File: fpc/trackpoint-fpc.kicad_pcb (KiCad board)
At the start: 2 copper layers, 10.2 x 25.4 mm, 3 parts, among them P1 CONN_8, P2 CONN_5, P3 CONN_8

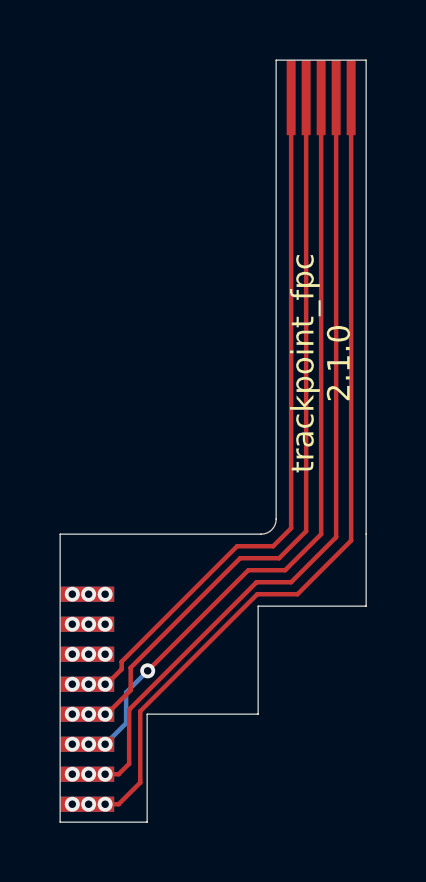
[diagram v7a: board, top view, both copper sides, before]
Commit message: Update FPC CAD and bump its version to 2.2.0
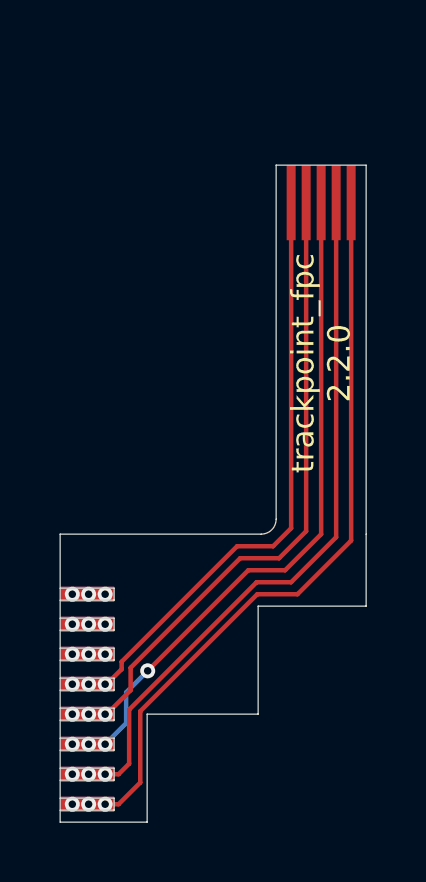
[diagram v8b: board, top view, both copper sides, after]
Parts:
- moved P2 3.50 mm to (198.3, 128.7)
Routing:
- net /DATA: track 22.8 -> 18.2 mm
- net /VCC: track 28.0 -> 23.4 mm
- net /RESET: track 25.3 -> 20.8 mm
- net /GND: track 26.6 -> 22.1 mm
- net /CLK: track 23.9 -> 19.5 mm
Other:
- board size 10.2 x 25.4 mm -> 10.2 x 21.9 mm
- board text added: "trackpoint_fpc 2.2.0"
- board text removed: "trackpoint_fpc 2.1.0"
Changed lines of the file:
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@@
   (general
     (thickness 1.6)
-    (drawings 30)
+    (drawings 54)
     (tracks 59)
     (zones 0)
@@
   (title_block
     (title "UHK Trackpoint FPC")
-    (rev 2.1.0)
+    (rev 2.2.0)
     (company "Ultimate Gadget Laboratories Kft.")
   )
@@
   )
   (module UGL:Trackpoint_FPC_5x0.5_pads (layer F.Cu)
-    (at 198.3 125.15)
+    (at 198.3 128.65)
     (attr smd)
     (fp_text reference P2 (at 0 3.65) (layer F.SilkS) hide
@@
   )
   (gr_line (start 199.8 128.9) (end 196.8 128.9) (layer Cmts.User) (width 0.05))
-  (gr_text "trackpoint_fpc\n2.1.0" (at 198.3 134 90) (layer F.SilkS)
+  (gr_text "trackpoint_fpc\n2.2.0" (at 198.3 134 90) (layer F.SilkS)
     (effects (font (size 0.75 0.75) (thickness 0.15)))
   )
-  (gr_text "Stiffener BOTTOM" (at 206.6 126.4) (layer Dwgs.User)
+  (gr_text "Stiffener BOTTOM" (at 206.6 129.9) (layer Dwgs.User)
     (effects (font (size 1 1) (thickness 0.15)))
   )
-  (gr_text "5.00 mm" (at 205.35 118.8 90) (layer Dwgs.User)
+  (gr_text "5.00 mm" (at 205.35 122.3 90) (layer Dwgs.User)
     (effects (font (size 1 1) (thickness 0.15)))
   )
-  (gr_line (start 206.25 123.1) (end 206.35 123.1) (layer Dwgs.User) (width 0.15))
-  (gr_line (start 206.15 123) (end 206.45 123) (layer Dwgs.User) (width 0.15))
-  (gr_line (start 206.2 129.6) (end 206.4 129.6) (layer Dwgs.User) (width 0.15))
-  (gr_line (start 206.15 129.7) (end 206.4 129.7) (layer Dwgs.User) (width 0.15))
-  (gr_line (start 206.5 129.8) (end 206.1 129.8) (layer Dwgs.User) (width 0.15))
-  (gr_line (start 206.3 128.9) (end 206.5 129.8) (layer Dwgs.User) (width 0.15))
-  (gr_line (start 206.3 128.9) (end 206.1 129.8) (layer Dwgs.User) (width 0.15))
-  (gr_line (start 206.3 128.9) (end 206.3 131.45) (layer Dwgs.User) (width 0.15))
-  (gr_line (start 206.5 122.85) (end 206.1 122.85) (layer Dwgs.User) (width 0.15))
-  (gr_line (start 206.3 123.9) (end 206.5 122.85) (layer Dwgs.User) (width 0.15))
-  (gr_line (start 206.3 123.9) (end 206.1 122.85) (layer Dwgs.User) (width 0.15))
-  (gr_line (start 206.3 123.9) (end 206.3 115.2) (layer Dwgs.User) (width 0.15))
-  (gr_line (start 199.8 128.9) (end 207.3 128.9) (layer Dwgs.User) (width 0.15))
-  (gr_line (start 199.8 123.9) (end 207.3 123.9) (layer Dwgs.User) (width 0.15))
-  (gr_line (start 199.8 123.8975) (end 199.8 139.6975) (angle 90) (layer Edge.Cuts) (width 0.01))
-  (gr_line (start 196.8 123.8975) (end 196.8 139.1975) (angle 90) (layer Edge.Cuts) (width 0.01))
+  (gr_line (start 206.25 126.6) (end 206.35 126.6) (layer Dwgs.User) (width 0.15))
+  (gr_line (start 206.15 126.5) (end 206.45 126.5) (layer Dwgs.User) (width 0.15))
+  (gr_line (start 206.2 133.1) (end 206.4 133.1) (layer Dwgs.User) (width 0.15))
+  (gr_line (start 206.15 133.2) (end 206.4 133.2) (layer Dwgs.User) (width 0.15))
+  (gr_line (start 206.5 133.3) (end 206.1 133.3) (layer Dwgs.User) (width 0.15))
+  (gr_line (start 206.3 132.4) (end 206.5 133.3) (layer Dwgs.User) (width 0.15))
+  (gr_line (start 206.3 132.4) (end 206.1 133.3) (layer Dwgs.User) (width 0.15))
+  (gr_line (start 206.3 132.4) (end 206.3 134.95) (layer Dwgs.User) (width 0.15))
+  (gr_line (start 206.5 126.35) (end 206.1 126.35) (layer Dwgs.User) (width 0.15))
+  (gr_line (start 206.3 127.4) (end 206.5 126.35) (layer Dwgs.User) (width 0.15))
+  (gr_line (start 206.3 127.4) (end 206.1 126.35) (layer Dwgs.User) (width 0.15))
+  (gr_line (start 206.3 127.4) (end 206.3 118.7) (layer Dwgs.User) (width 0.15))
+  (gr_line (start 199.8 132.4) (end 207.3 132.4) (layer Dwgs.User) (width 0.15))
+  (gr_line (start 199.8 127.4) (end 207.3 127.4) (layer Dwgs.User) (width 0.15))
+  (gr_line (start 189.6 147.8975) (end 191.4 147.8975) (angle 90) (layer Edge.Cuts) (width 0.01))
+  (gr_line (start 191.4 147.4975) (end 189.6 147.4975) (angle 90) (layer Edge.Cuts) (width 0.01))
+  (gr_line (start 191.4 147.8975) (end 191.4 147.4975) (angle 90) (layer Edge.Cuts) (width 0.01))
+  (gr_line (start 189.6 145.8975) (end 191.4 145.8975) (angle 90) (layer Edge.Cuts) (width 0.01))
+  (gr_line (start 191.4 145.4975) (end 189.6 145.4975) (angle 90) (layer Edge.Cuts) (width 0.01))
+  (gr_line (start 191.4 145.8975) (end 191.4 145.4975) (angle 90) (layer Edge.Cuts) (width 0.01))
+  (gr_line (start 189.6 143.8975) (end 191.4 143.8975) (angle 90) (layer Edge.Cuts) (width 0.01))
+  (gr_line (start 191.4 143.4975) (end 189.6 143.4975) (angle 90) (layer Edge.Cuts) (width 0.01))
+  (gr_line (start 191.4 143.8975) (end 191.4 143.4975) (angle 90) (layer Edge.Cuts) (width 0.01))
+  (gr_line (start 189.6 141.8975) (end 191.4 141.8975) (angle 90) (layer Edge.Cuts) (width 0.01))
+  (gr_line (start 191.4 141.4975) (end 189.6 141.4975) (angle 90) (layer Edge.Cuts) (width 0.01))
+  (gr_line (start 191.4 141.8975) (end 191.4 141.4975) (angle 90) (layer Edge.Cuts) (width 0.01))
+  (gr_line (start 189.6 142.8975) (end 191.4 142.8975) (angle 90) (layer Edge.Cuts) (width 0.01))
+  (gr_line (start 191.4 142.4975) (end 189.6 142.4975) (angle 90) (layer Edge.Cuts) (width 0.01))
+  (gr_line (start 191.4 142.8975) (end 191.4 142.4975) (angle 90) (layer Edge.Cuts) (width 0.01))
+  (gr_line (start 189.6 144.8975) (end 191.4 144.8975) (angle 90) (layer Edge.Cuts) (width 0.01))
+  (gr_line (start 191.4 144.4975) (end 189.6 144.4975) (angle 90) (layer Edge.Cuts) (width 0.01))
+  (gr_line (start 191.4 144.8975) (end 191.4 144.4975) (angle 90) (layer Edge.Cuts) (width 0.01))
+  (gr_line (start 189.6 146.8975) (end 191.4 146.8975) (angle 90) (layer Edge.Cuts) (width 0.01))
+  (gr_line (start 191.4 146.4975) (end 189.6 146.4975) (angle 90) (layer Edge.Cuts) (width 0.01))
+  (gr_line (start 191.4 146.8975) (end 191.4 146.4975) (angle 90) (layer Edge.Cuts) (width 0.01))
+  (gr_line (start 189.6 148.8975) (end 191.4 148.8975) (angle 90) (layer Edge.Cuts) (width 0.01))
+  (gr_line (start 191.4 148.4975) (end 189.6 148.4975) (angle 90) (layer Edge.Cuts) (width 0.01))
+  (gr_line (start 191.4 148.8975) (end 191.4 148.4975) (angle 90) (layer Edge.Cuts) (width 0.01))
+  (gr_line (start 199.8 127.3975) (end 199.8 139.6975) (angle 90) (layer Edge.Cuts) (width 0.01))
+  (gr_line (start 196.8 127.3975) (end 196.8 139.1975) (angle 90) (layer Edge.Cuts) (width 0.01))
   (gr_line (start 196.3 139.6975) (end 189.6 139.6975) (angle 90) (layer Edge.Cuts) (width 0.01))
   (gr_line (start 192.5 149.2975) (end 192.5 145.6975) (angle 90) (layer Edge.Cuts) (width 0.01))
@@
   (gr_line (start 199.8 142.0975) (end 199.8 139.6975) (angle 90) (layer Edge.Cuts) (width 0.01))
   (gr_line (start 196.2 142.0975) (end 199.8 142.0975) (angle 90) (layer Edge.Cuts) (width 0.01))
-  (gr_line (start 199.8 123.8975) (end 196.8 123.8975) (angle 90) (layer Edge.Cuts) (width 0.01))
   (gr_arc (start 196.300006 139.197511) (end 196.3 139.6975) (angle -90.00254177) (layer Edge.Cuts) (width 0.01))
+  (gr_line (start 199.8 127.3975) (end 196.8 127.3975) (angle 90) (layer Edge.Cuts) (width 0.01))
   (segment (start 197.512139 141.7) (end 199.3 139.912139) (width 0.15) (layer F.Cu) (net 1))
   (segment (start 192.26999 145.602227) (end 196.172217 141.7) (width 0.15) (layer F.Cu) (net 1))
@@
   (via (at 190.55 148.7) (size 0.5) (drill 0.25) (layers F.Cu B.Cu) (net 1))
   (segment (start 191.55 148.7) (end 191.1 148.7) (width 0.15) (layer F.Cu) (net 1))
-  (segment (start 199.3 139.912139) (end 199.3 125.15) (width 0.15) (layer F.Cu) (net 1))
+  (segment (start 199.3 139.912139) (end 199.3 129.7) (width 0.15) (layer F.Cu) (net 1))
   (segment (start 197.3 141.3) (end 198.8 139.8) (width 0.15) (layer F.Cu) (net 2))
   (segment (start 191.899991 145.547947) (end 196.147938 141.3) (width 0.15) (layer F.Cu) (net 2))
@@
   (via (at 191.1 147.7) (size 0.5) (drill 0.25) (layers F.Cu B.Cu) (net 2))
   (segment (start 191.55 147.7) (end 191.1 147.7) (width 0.15) (layer F.Cu) (net 2))
-  (segment (start 198.8 139.8) (end 198.8 125.25) (width 0.15) (layer F.Cu) (net 2))
+  (segment (start 198.8 139.8) (end 198.8 129.7) (width 0.15) (layer F.Cu) (net 2))
   (via (at 190.005 146.7) (size 0.5) (drill 0.25) (layers F.Cu B.Cu) (net 3))
   (via (at 190.55 146.7) (size 0.5) (drill 0.25) (layers F.Cu B.Cu) (net 3))
@@
   (segment (start 191.8 146) (end 191.8 144.971767) (width 0.15) (layer B.Cu) (net 3))
   (segment (start 191.1 146.7) (end 191.8 146) (width 0.15) (layer B.Cu) (net 3))
-  (segment (start 198.3 139.7) (end 198.3 125.2) (width 0.15) (layer F.Cu) (net 3))
+  (segment (start 198.3 139.7) (end 198.3 129.7) (width 0.15) (layer F.Cu) (net 3))
   (segment (start 196.9 140.5) (end 197.8 139.6) (width 0.15) (layer F.Cu) (net 4))
   (segment (start 195.6 140.5) (end 196.9 140.5) (width 0.15) (layer F.Cu) (net 4))
@@
   (via (at 190.55 145.7) (size 0.5) (drill 0.25) (layers F.Cu B.Cu) (net 4))
   (via (at 191.1 145.7) (size 0.5) (drill 0.25) (layers F.Cu B.Cu) (net 4))
-  (segment (start 197.8 139.6) (end 197.8 125.3) (width 0.15) (layer F.Cu) (net 4))
+  (segment (start 197.8 139.6) (end 197.8 129.7) (width 0.15) (layer F.Cu) (net 4))
   (segment (start 195.5 140.1) (end 196.7 140.1) (width 0.15) (layer F.Cu) (net 5))
   (segment (start 191.65 143.95) (end 195.5 140.1) (width 0.15) (layer F.Cu) (net 5))
@@
   (via (at 190.55 144.7) (size 0.5) (drill 0.25) (layers F.Cu B.Cu) (net 5))
   (via (at 191.1 144.7) (size 0.5) (drill 0.25) (layers F.Cu B.Cu) (net 5))
-  (segment (start 197.3 139.5) (end 197.3 125.15) (width 0.15) (layer F.Cu) (net 5))
+  (segment (start 197.3 139.5) (end 197.3 129.8) (width 0.15) (layer F.Cu) (net 5))
   (via (at 190.005 143.7) (size 0.5) (drill 0.25) (layers F.Cu B.Cu) (net 6))
   (via (at 190.55 143.7) (size 0.5) (drill 0.25) (layers F.Cu B.Cu) (net 6))
